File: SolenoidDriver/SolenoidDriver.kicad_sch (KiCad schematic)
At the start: 14 parts, among them J1 Conn_01x08_Pin, J2 Conn_01x08_Pin, Q1 BC818W, Q2 BC818W, Q3 BC818W, Q4 BC818W

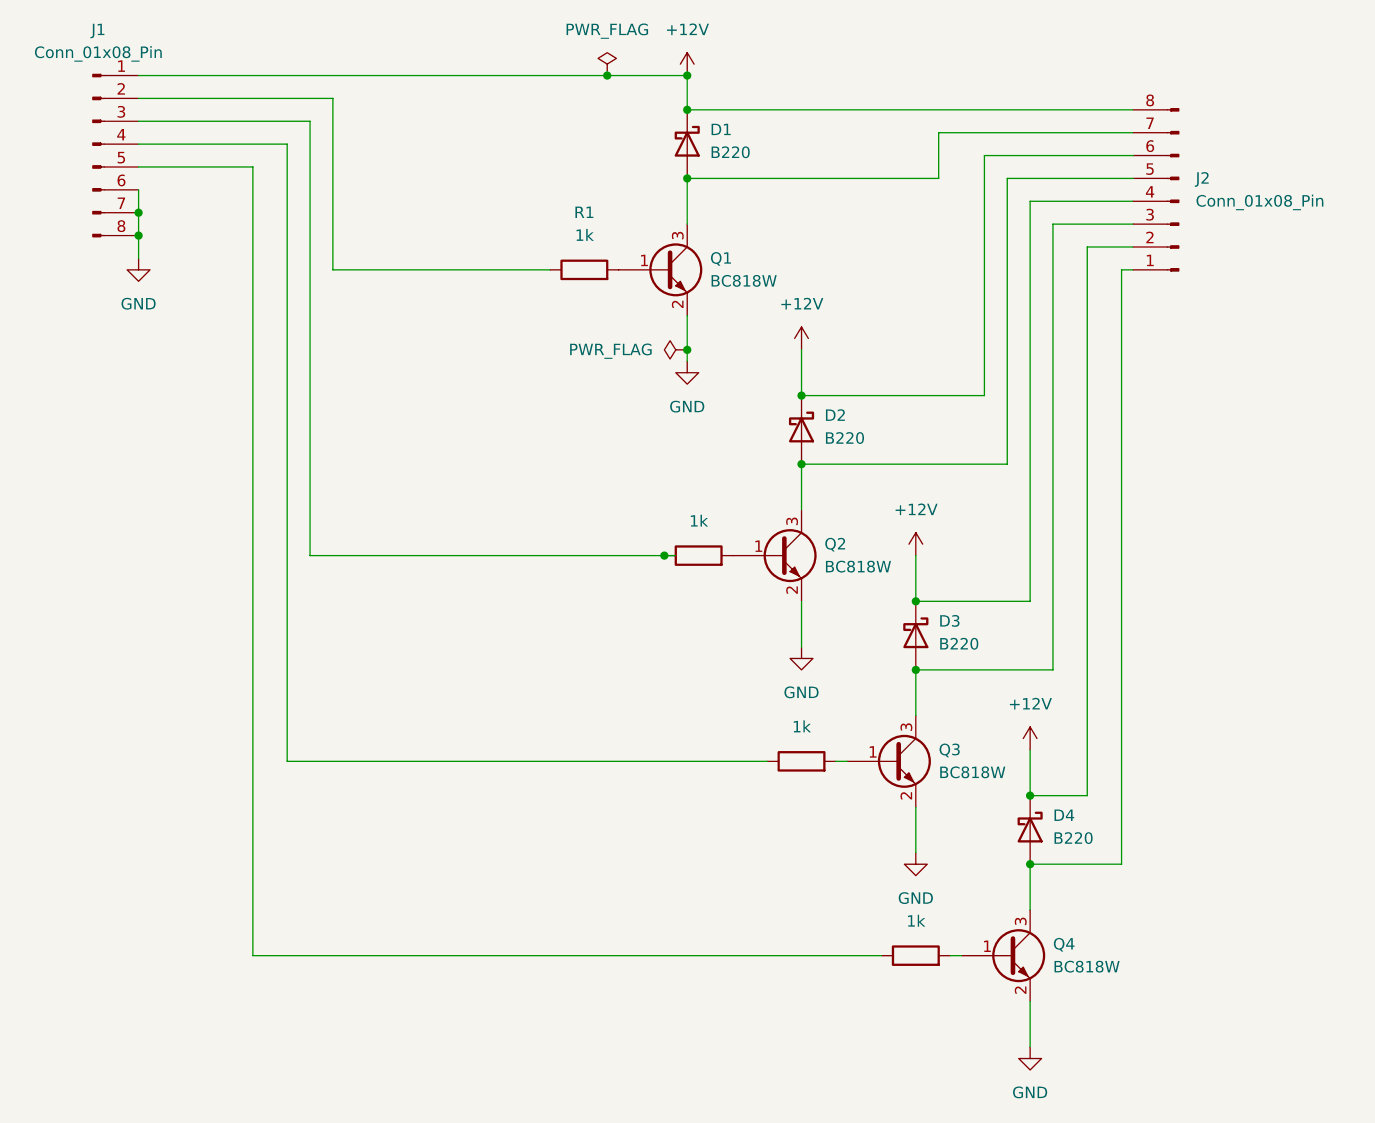
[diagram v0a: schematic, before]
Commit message: Added manufacturing files for solenoid driver and 555 timer
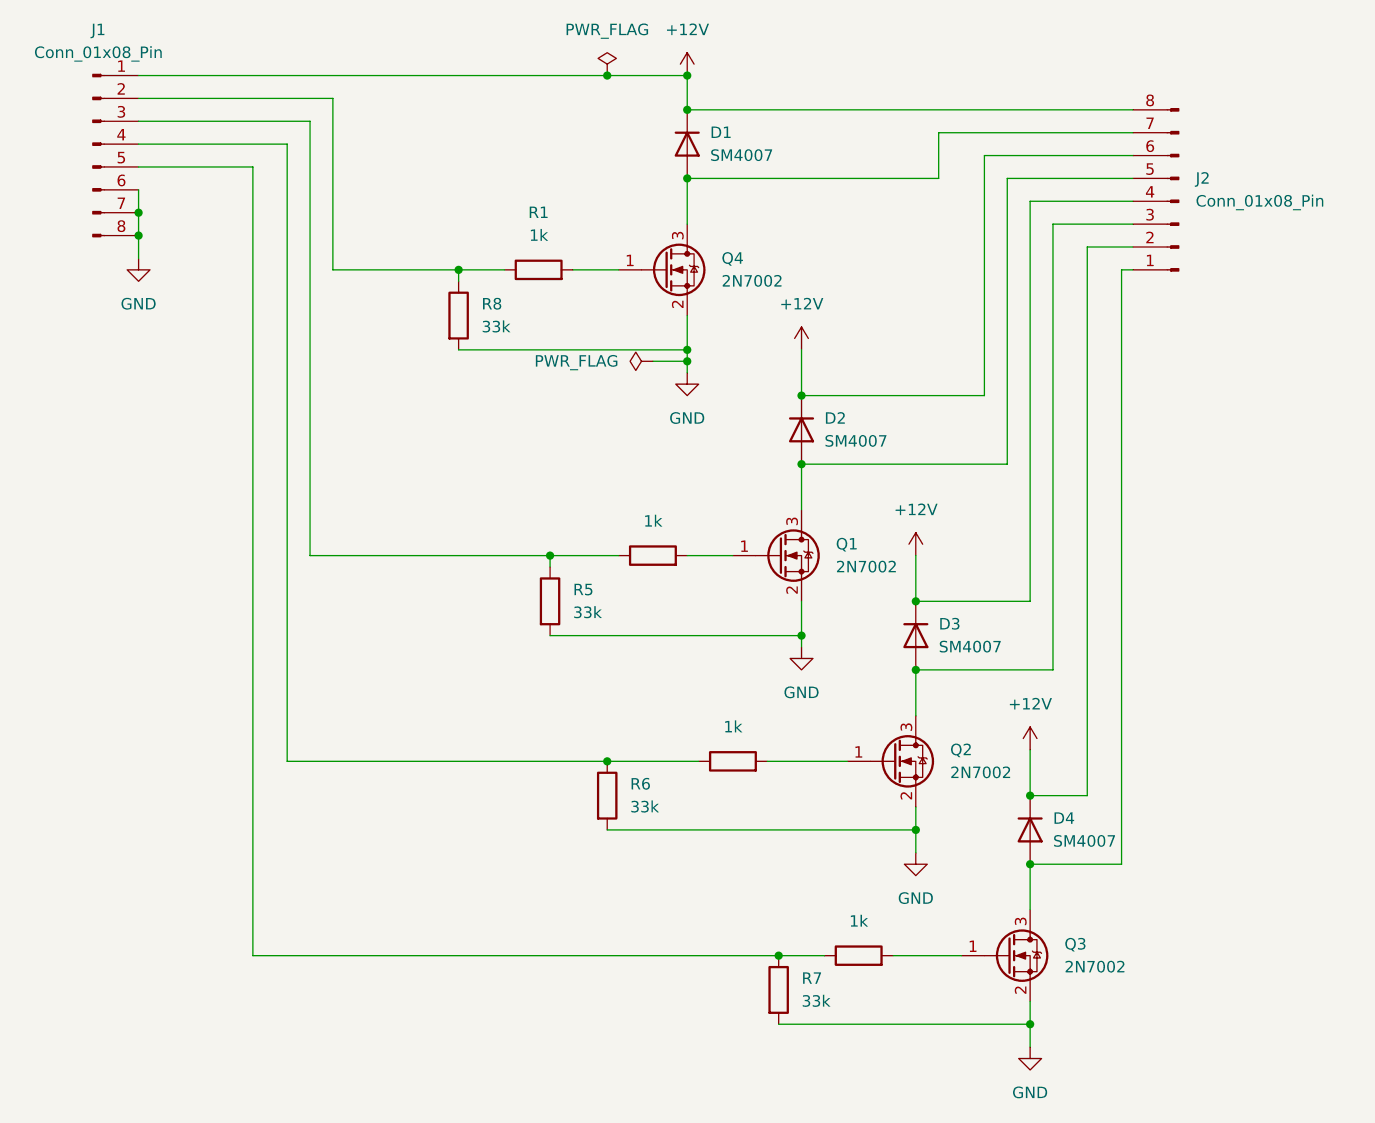
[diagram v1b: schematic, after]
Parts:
- removed D1, D2, D3, D4: B220, Diode_SMD:D_SMB, symbol Diode:B220
- removed Q1, Q2, Q3, Q4: BC818W, Package_TO_SOT_SMD:SOT-323_SC-70, symbol Transistor_BJT:BC818W
- added D1, D2, D3, D4: SM4007, Diode_SMD:D_MELF, symbol Diode:SM4007
- added Q1, Q2, Q3, Q4: 2N7002, Package_TO_SOT_SMD:SOT-23, symbol Transistor_FET:2N7002
- added R5, R6, R7, R8: 33k, Resistor_SMD:R_0603_1608Metric, symbol Device:R
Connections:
- net +12V: now also D1.1 (K), D2.1 (K), D3.1 (K), D4.1 (K)
- net GND: now also Q1.2 (S), Q2.2 (S), Q3.2 (S), Q4.2 (S), R5.2, R6.2, R7.2, R8.2
- net at J2.1 (Pin_1): now also D4.2 (A), Q3.3 (D)
- net at R2.2: now also Q1.1 (G)
- net at J2.5 (Pin_5): now also D2.2 (A), Q1.3 (D)
- net at J1.3 (Pin_3), R2.1: now also R5.1
- net at J2.3 (Pin_3): now also D3.2 (A), Q2.3 (D)
- net at J1.2 (Pin_2), R1.1: now also R8.1
- net at R1.2: now also Q4.1 (G)
- net at J1.4 (Pin_4), R3.1: now also R6.1
- net at R3.2: now also Q2.1 (G)
- net at J1.5 (Pin_5), R4.1: now also R7.1
- net at R4.2: now also Q3.1 (G)
- net at J2.7 (Pin_7): now also D1.2 (A), Q4.3 (D)
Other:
- moved on the sheet: R1
